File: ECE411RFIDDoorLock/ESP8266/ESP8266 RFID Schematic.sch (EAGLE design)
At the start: 30 parts, among them M1 SERVO, Q3 DMG341, T1 600mA/40V, T2 600mA/40V, U3 AP2112-3.3, X1 ESP-12E, X4 20329

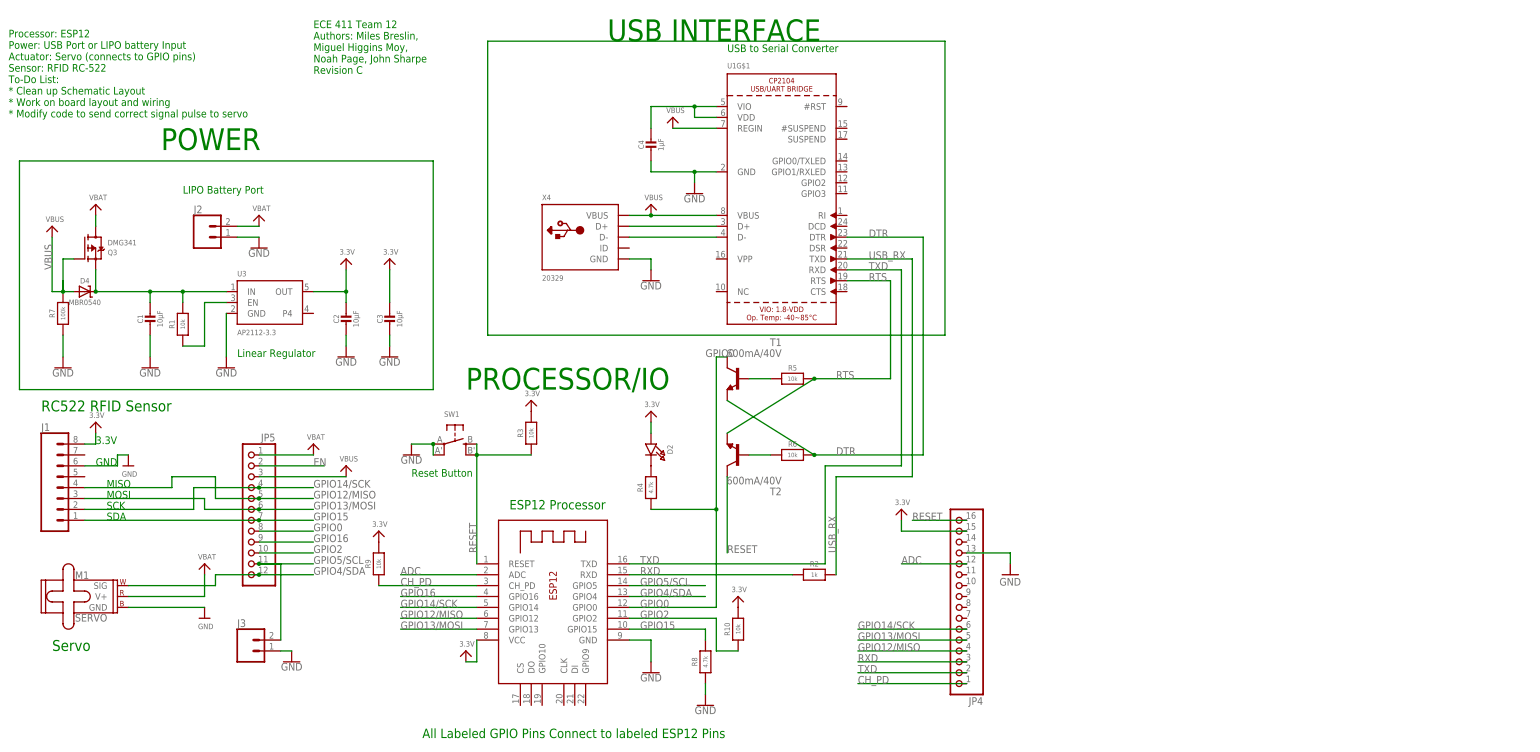
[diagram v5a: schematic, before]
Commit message: added more ground stitching, iso on top pour, info layer on schematic
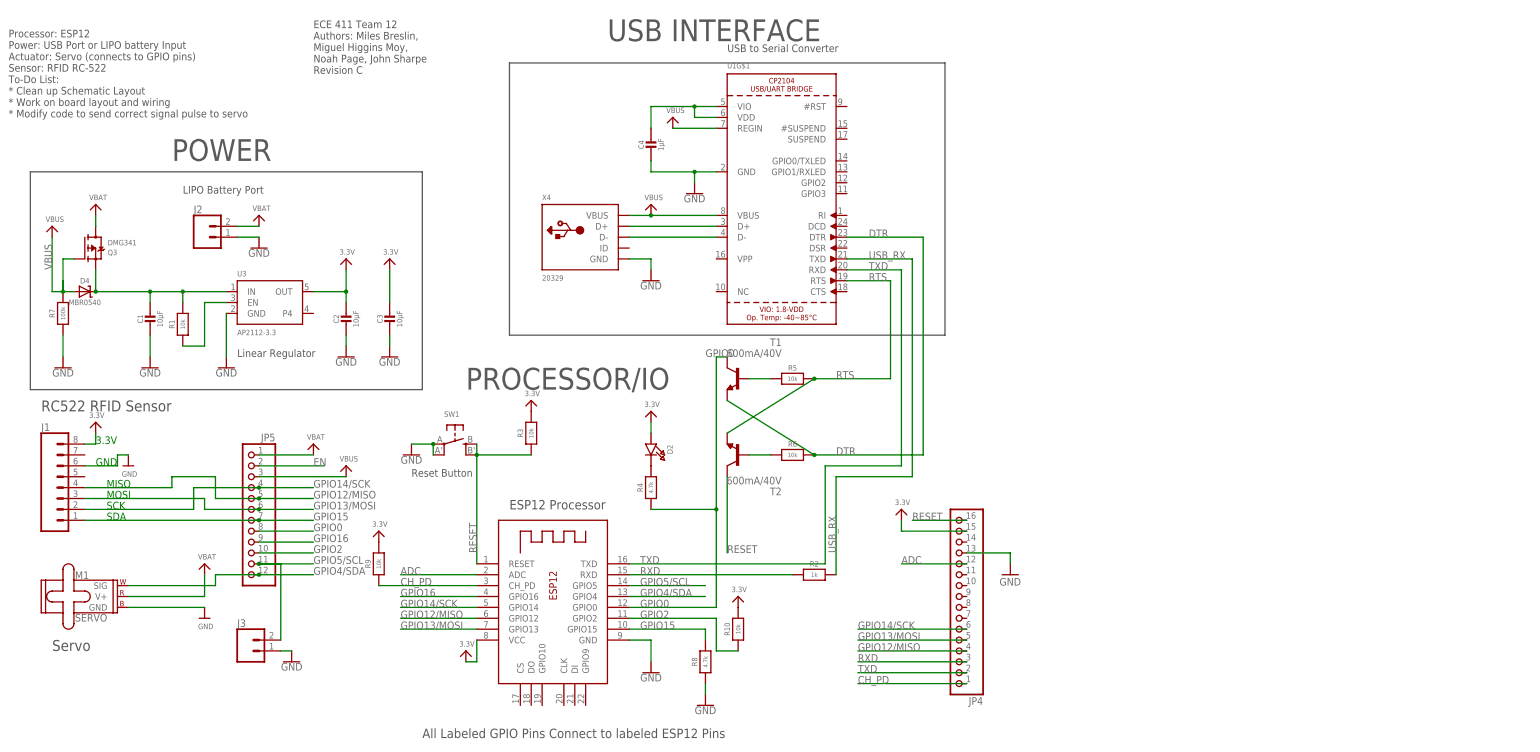
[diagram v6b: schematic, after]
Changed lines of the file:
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@@
 <sheet>
 <plain>
-<text x="106.68" y="5.08" size="2.1844" layer="91">All Labeled GPIO Pins Connect to labeled ESP12 Pins</text>
-<text x="127" y="58.42" size="2.1844" layer="91">ESP12 Processor</text>
-<text x="104.14" y="66.04" size="1.778" layer="91">Reset Button</text>
-<text x="177.8" y="165.1" size="1.778" layer="91">USB to Serial Converter</text>
-<text x="10.16" y="149.86" size="1.778" layer="91">Processor: ESP12
+<text x="106.68" y="5.08" size="2.1844" layer="97">All Labeled GPIO Pins Connect to labeled ESP12 Pins</text>
+<text x="127" y="58.42" size="2.1844" layer="97">ESP12 Processor</text>
+<text x="104.14" y="66.04" size="1.778" layer="97">Reset Button</text>
+<text x="177.8" y="165.1" size="1.778" layer="97">USB to Serial Converter</text>
+<text x="10.16" y="149.86" size="1.778" layer="97">Processor: ESP12
 Power: USB Port or LIPO battery Input
 Actuator: Servo (connects to GPIO pins)
@@
 * Modify code to send correct signal pulse to servo
 </text>
-<text x="45.72" y="142.24" size="5.08" layer="91">POWER</text>
-<text x="149.86" y="167.64" size="5.08" layer="91">USB INTERFACE</text>
-<text x="116.84" y="86.36" size="5.08" layer="91">PROCESSOR/IO</text>
+<text x="48.26" y="139.7" size="5.08" layer="97">POWER</text>
+<text x="149.86" y="167.64" size="5.08" layer="97">USB INTERFACE</text>
+<text x="116.84" y="86.36" size="5.08" layer="97">PROCESSOR/IO</text>
 <text x="33.02" y="55.88" size="1.778" layer="91">SDA</text>
 <text x="33.02" y="58.42" size="1.778" layer="91">SCK</text>
@@
 <text x="30.48" y="68.58" size="1.778" layer="91">GND</text>
 <text x="30.48" y="73.66" size="1.778" layer="91">3.3V</text>
-<text x="17.78" y="81.28" size="2.54" layer="91">RC522 RFID Sensor</text>
-<text x="20.32" y="25.4" size="2.54" layer="91">Servo</text>
-<text x="63.5" y="93.98" size="1.778" layer="91">Linear Regulator</text>
-<text x="50.8" y="132.08" size="1.778" layer="91">LIPO Battery Port</text>
-<text x="81.28" y="160.02" size="1.778" layer="91">ECE 411 Team 12
+<text x="17.78" y="81.28" size="2.54" layer="97">RC522 RFID Sensor</text>
+<text x="20.32" y="25.4" size="2.54" layer="97">Servo</text>
+<text x="63.5" y="93.98" size="1.778" layer="97">Linear Regulator</text>
+<text x="50.8" y="132.08" size="1.778" layer="97">LIPO Battery Port</text>
+<text x="81.28" y="160.02" size="1.778" layer="97">ECE 411 Team 12
 Authors: Miles Breslin,
 Miguel Higgins Moy,
 Noah Page, John Sharpe
 Revision C</text>
+<wire x1="15.24" y1="137.16" x2="15.24" y2="86.36" width="0.1524" layer="97"/>
+<wire x1="15.24" y1="86.36" x2="106.68" y2="86.36" width="0.1524" layer="97"/>
+<wire x1="106.68" y1="86.36" x2="106.68" y2="137.16" width="0.1524" layer="97"/>
+<wire x1="106.68" y1="137.16" x2="15.24" y2="137.16" width="0.1524" layer="97"/>
+<wire x1="127" y1="162.56" x2="127" y2="99.06" width="0.1524" layer="97"/>
+<wire x1="127" y1="99.06" x2="228.6" y2="99.06" width="0.1524" layer="97"/>
+<wire x1="228.6" y1="99.06" x2="228.6" y2="162.56" width="0.1524" layer="97"/>
+<wire x1="228.6" y1="162.56" x2="127" y2="162.56" width="0.1524" layer="97"/>
 </plain>
 <instances>
@@
 </segment>
 </net>
-<net name="N$12" class="0">
-<segment>
-<wire x1="109.22" y1="86.36" x2="109.22" y2="139.7" width="0.1524" layer="91"/>
-<wire x1="109.22" y1="86.36" x2="12.7" y2="86.36" width="0.1524" layer="91"/>
-<wire x1="12.7" y1="86.36" x2="12.7" y2="139.7" width="0.1524" layer="91"/>
-<wire x1="12.7" y1="139.7" x2="109.22" y2="139.7" width="0.1524" layer="91"/>
-</segment>
-</net>
-<net name="N$13" class="0">
-<segment>
-<wire x1="121.92" y1="99.06" x2="228.6" y2="99.06" width="0.1524" layer="91"/>
-<wire x1="228.6" y1="99.06" x2="228.6" y2="167.64" width="0.1524" layer="91"/>
-<wire x1="228.6" y1="167.64" x2="121.92" y2="167.64" width="0.1524" layer="91"/>
-<wire x1="121.92" y1="167.64" x2="121.92" y2="99.06" width="0.1524" layer="91"/>
-</segment>
-</net>

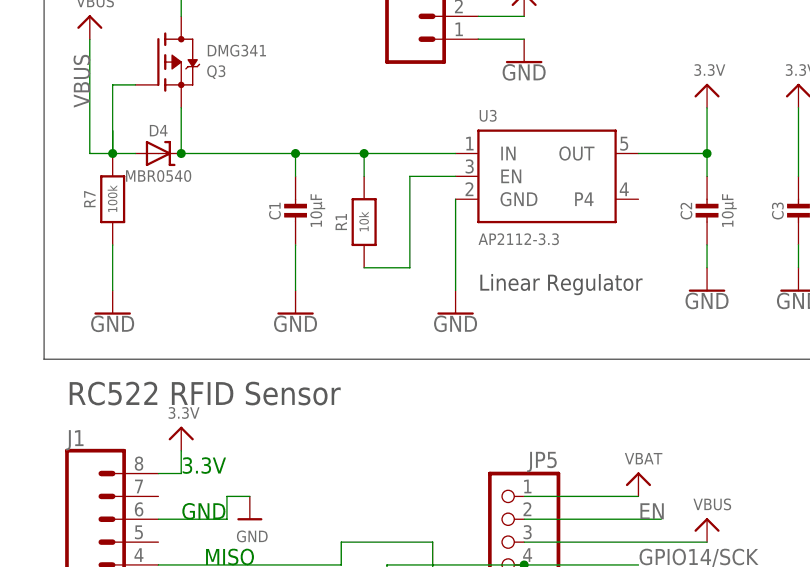
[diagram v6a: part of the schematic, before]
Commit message: routed EN
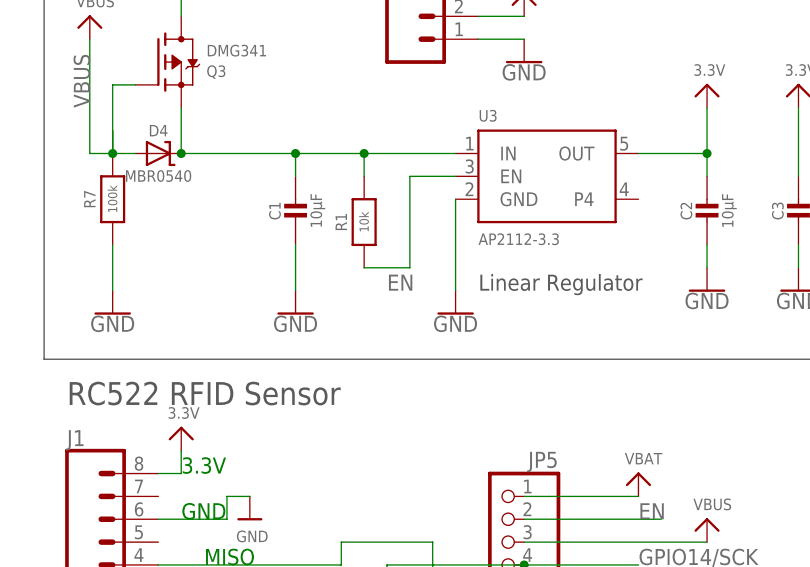
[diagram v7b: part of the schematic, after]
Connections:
- removed net N$10: R1.1, U3.EN
- net EN: now also R1.1, U3.EN
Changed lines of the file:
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@@
-</segment>
-</net>
-<net name="N$10" class="0">
-<segment>
-<pinref part="U3" gate="G$1" pin="EN"/>
-<wire x1="55.88" y1="106.68" x2="60.96" y2="106.68" width="0.1524" layer="91"/>
-<pinref part="R1" gate="G$1" pin="1"/>
-<wire x1="50.8" y1="96.52" x2="55.88" y2="96.52" width="0.1524" layer="91"/>
-<wire x1="55.88" y1="96.52" x2="55.88" y2="106.68" width="0.1524" layer="91"/>
 </segment>
 </net>
@@
 <label x="81.28" y="68.58" size="1.778" layer="95"/>
 </segment>
+<segment>
+<pinref part="U3" gate="G$1" pin="EN"/>
+<wire x1="55.88" y1="106.68" x2="60.96" y2="106.68" width="0.1524" layer="91"/>
+<pinref part="R1" gate="G$1" pin="1"/>
+<wire x1="50.8" y1="96.52" x2="55.88" y2="96.52" width="0.1524" layer="91"/>
+<wire x1="55.88" y1="96.52" x2="55.88" y2="106.68" width="0.1524" layer="91"/>
+<label x="53.34" y="93.98" size="1.778" layer="95"/>
+</segment>
 </net>

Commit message: Some VIA work and clean up
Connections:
- net GND: now also U1G$2.TP
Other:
- note added: "Battery Port"
- note removed: "LIPO Battery Port"
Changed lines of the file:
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@@
 <part name="U$13" library="microbuilder" deviceset="VBUS" device=""/>
 <part name="U$10" library="microbuilder" deviceset="VBUS" device=""/>
+<part name="GND14" library="SparkFun-PowerSymbols" deviceset="GND" device=""/>
 </parts>
 <sheets>
@@
 <text x="20.32" y="25.4" size="2.54" layer="97">Servo</text>
 <text x="63.5" y="93.98" size="1.778" layer="97">Linear Regulator</text>
-<text x="50.8" y="132.08" size="1.778" layer="97">LIPO Battery Port</text>
+<text x="50.8" y="132.08" size="1.778" layer="97">Battery Port</text>
 <text x="81.28" y="160.02" size="1.778" layer="97">ECE 411 Team 12
 Authors: Miles Breslin,
@@
 <attribute name="VALUE" x="163.576" y="150.876" size="1.27" layer="96"/>
 </instance>
+<instance part="U1" gate="G$2" x="218.44" y="149.86" smashed="yes">
+<attribute name="NAME" x="213.36" y="156.21" size="1.778" layer="95"/>
+</instance>
+<instance part="GND14" gate="1" x="218.44" y="139.7" smashed="yes">
+<attribute name="VALUE" x="218.44" y="139.446" size="1.778" layer="96" align="top-center"/>
+</instance>
 </instances>
 <busses>
@@
 <wire x1="172.72" y1="15.24" x2="172.72" y2="17.78" width="0.1524" layer="91"/>
 </segment>
+<segment>
+<pinref part="GND14" gate="1" pin="GND"/>
+<pinref part="U1" gate="G$2" pin="TP"/>
+</segment>
 </net>
 <net name="GPIO14/SCK" class="0">
@@
 </segment>
 <segment>
-<wire x1="68.58" y1="45.72" x2="81.28" y2="45.72" width="0.1524" layer="91"/>
+<wire x1="68.58" y1="45.72" x2="73.66" y2="45.72" width="0.1524" layer="91"/>
 <label x="81.28" y="45.72" size="1.778" layer="95"/>
 <pinref part="JP5" gate="G$1" pin="11"/>
+<wire x1="73.66" y1="45.72" x2="81.28" y2="45.72" width="0.1524" layer="91"/>
 <wire x1="68.58" y1="45.72" x2="73.66" y2="45.72" width="0.1524" layer="91"/>
 <wire x1="73.66" y1="45.72" x2="73.66" y2="27.94" width="0.1524" layer="91"/>
 <junction x="68.58" y="45.72"/>
 <pinref part="J3" gate="G$1" pin="2"/>
-</segment>
-</net>
+<junction x="73.66" y="45.72"/>
+</segment>
+</net>
